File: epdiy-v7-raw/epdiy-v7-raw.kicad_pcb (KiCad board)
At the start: 4 copper layers, 128.4 x 74.9 mm, 110 parts, among them CN1 WP27D-S050VA3-R15000, IC1 MPU-6500, J1 USB_C_Receptacle_USB2.0, J2 EXTENSION_HEADER, J3 SIGNALS_HEADER, J5 CONN_BAT, J7 ESP_HDR, Q1 AO3401A, SW1 TC-0522C-1.7-160G, SW2 TC-0522C-1.7-160G, U1 RT9080-33GJ5, U10 ED060XC5, U11 TP4056, U3 TPS651851RSLR, U4 USBLC6-2P6, U8 ESP32-S3-WROOM-1, Y1 RV-3032-C7

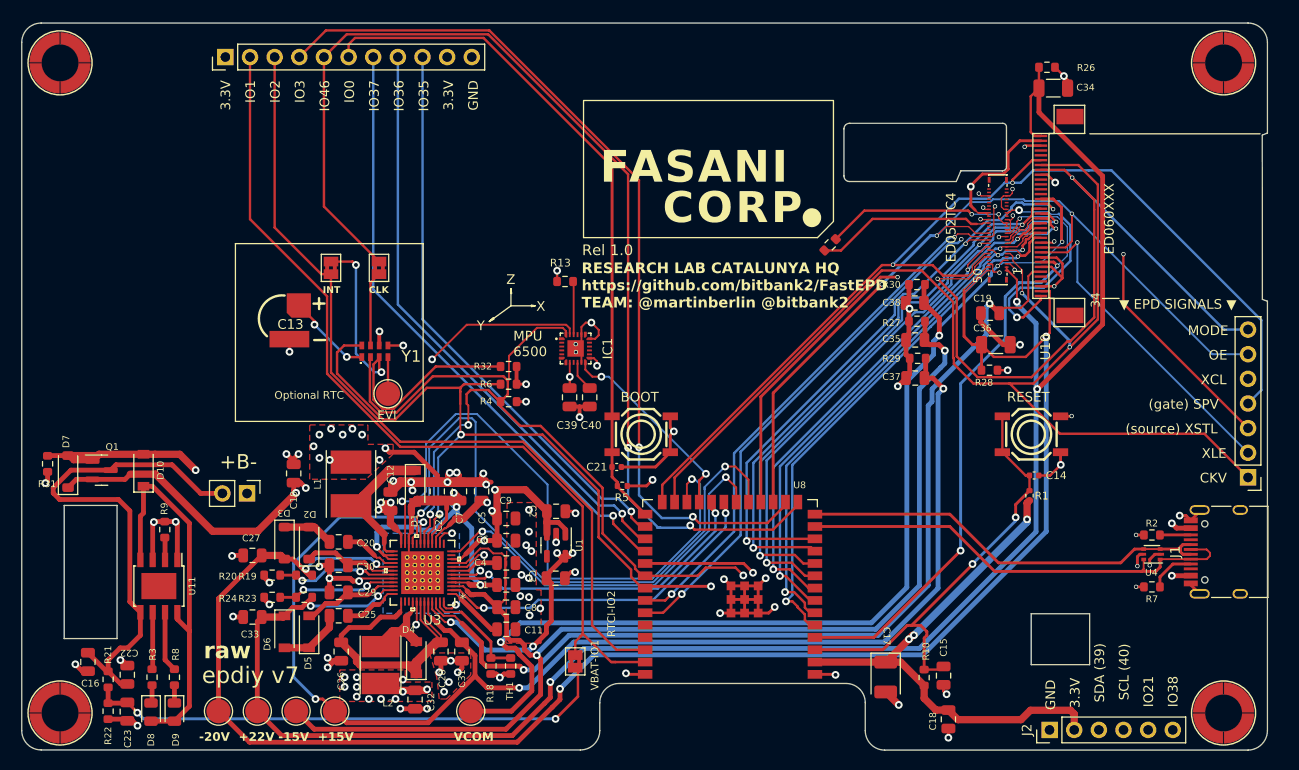
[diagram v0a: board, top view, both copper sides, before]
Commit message: Add MicroSD and fab files v1.0
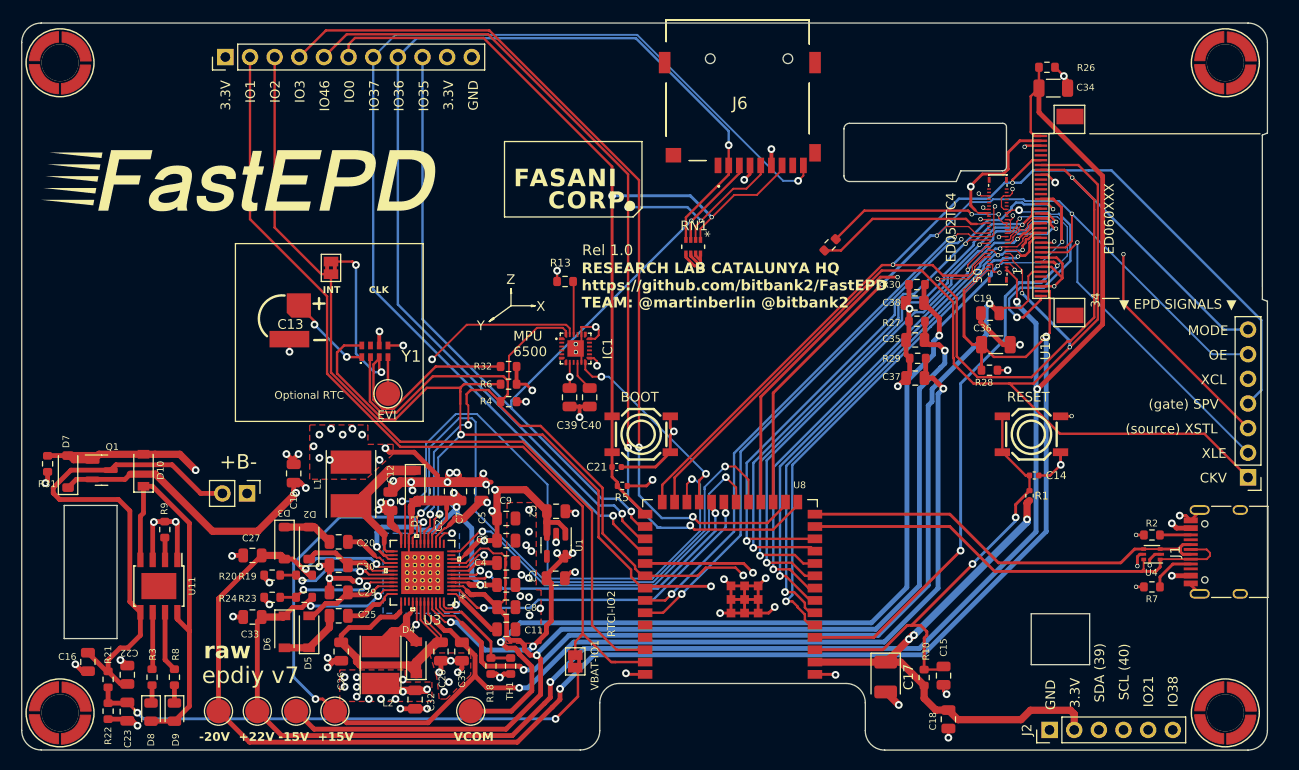
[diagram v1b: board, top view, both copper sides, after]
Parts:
- removed JP3: RTCCLK_GPIO1, Jumper:SolderJumper-2_P1.3mm_Bridged2Bar_Pad1.0x1.5mm
- added J6: THD2528-11SD-GF, footprints:MicroSD_THD252811SDGF, F.Cu at (131.8, 54.6)
- added RN1: R_Pack04, footprints:RESN_F392JTCE_UNR_SD-pullup, F.Cu at (127.2, 70.7)
- R3, R8: value 1k -> 2.4k
- R4, R6: value 10k -> 5.1k
- moved H2 0.18 mm to (182.1, 51.8)
- moved H4 0.18 mm to (182.1, 118.8)
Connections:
- Y1 pad 7: /RTC_CLK -> unconnected-(Y1-CLKOUT-Pad7)
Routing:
- net /GPIO_37: track 63.6 -> 116.4 mm, vias 1 -> 2
- net /GPIO_36: track 61.4 -> 113.3 mm, vias 1 -> 2
- net /GPIO_35: track 59.2 -> 96.0 mm, vias 1 -> 2
- net 3.3V: track 106.1 -> 140.6 mm, vias 14 -> 16
- net /IO0: track 71.5 -> 95.2 mm, vias 0 -> 2
- net /RTC_CLK: track 7.71 -> 0.00 mm
- net /GPIO_3: track 115.8 -> 111.8 mm, vias 2 -> 4
- net GND: track 200.0 -> 201.3 mm, vias 98 -> 99

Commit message: Update v7 raw
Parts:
- added R12: 10K, Resistor_SMD:R_0603_1608Metric, F.Cu at (180.8, 113.2)
- added R14: 10K, Resistor_SMD:R_0603_1608Metric, F.Cu at (62.5, 61.4)
- added R15: 10K, Resistor_SMD:R_0603_1608Metric, F.Cu at (62.5, 74.3)
- added SW3: K2-1806SQ-A2DW-04, footprints:C5143621_KEY-SMD_TS24ZJ, F.Cu at (184.5, 112.3)
- added SW4: K2-1806SQ-A2DW-04, footprints:C5143621_KEY-SMD_TS24ZJ, F.Cu at (59.8, 63.2)
- added SW5: K2-1806SQ-A2DW-04, footprints:C5143621_KEY-SMD_TS24ZJ, F.Cu at (59.8, 76.0)
- moved SW1 17.6 mm to (144.5, 88.5), turned to -90 degrees
- moved SW2 1.89 mm to (120.8, 88.5), turned to -90 degrees
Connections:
- SW1 pad 1: /EN -> GND
- SW1 pad 4: GND -> /EN
- SW2 pad 1: /IO0 -> GND
- SW2 pad 4: GND -> /IO0
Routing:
- net /GPIO_38: track 60.4 -> 132.6 mm, vias 1 -> 3
- net /GPIO_3: track 111.8 -> 173.2 mm
- net /GPIO_46: track 92.5 -> 127.9 mm
- net /EN: track 47.0 -> 65.9 mm
- net GND: track 201.3 -> 213.7 mm, vias 99 -> 102
- net Net-(R14-Pad1): track 0.00 -> 2.38 mm
- net Net-(R12-Pad1): track 0.00 -> 2.15 mm
- net Net-(R15-Pad1): track 0.00 -> 2.08 mm

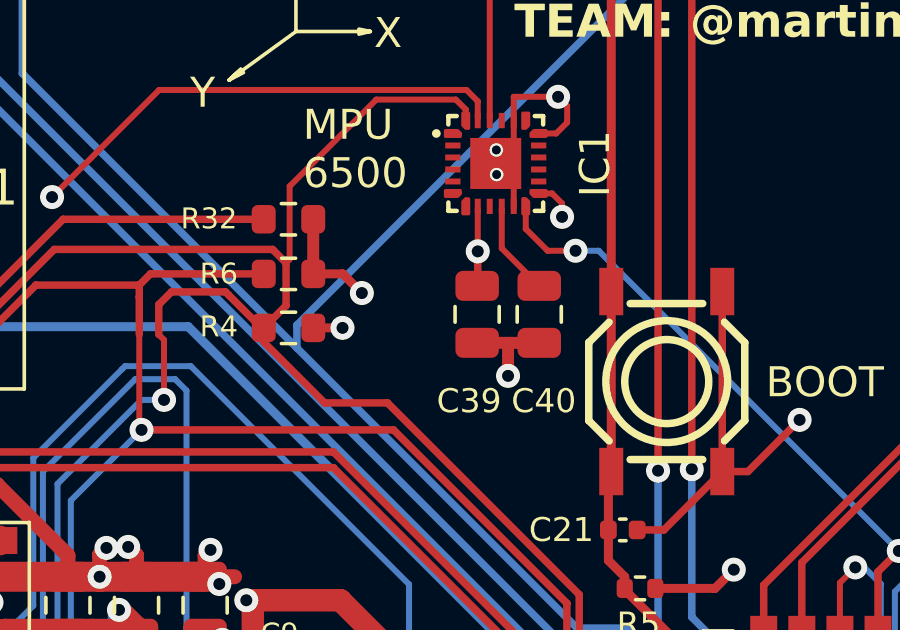
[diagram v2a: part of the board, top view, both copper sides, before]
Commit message: 1.1 corrected IMU to 0x69
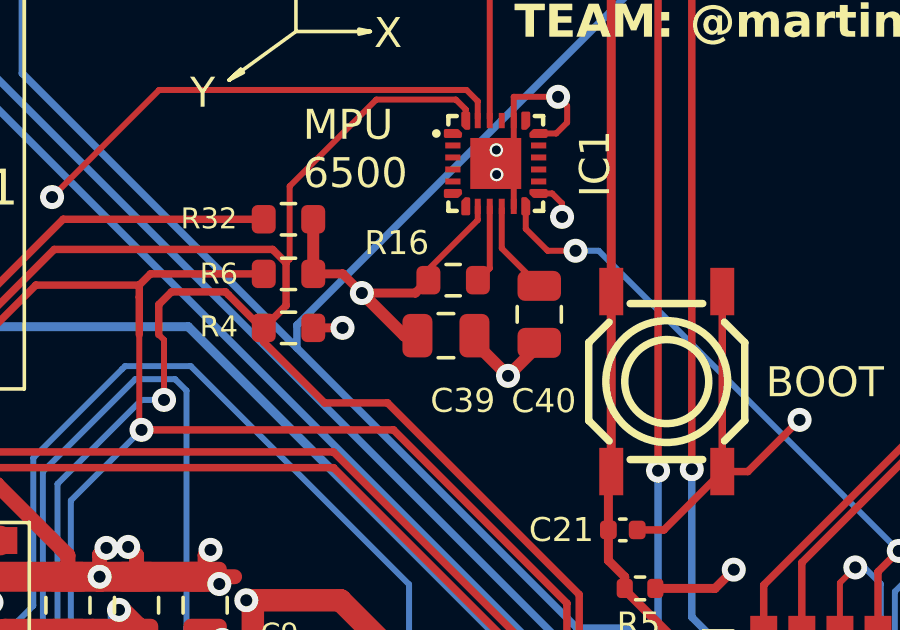
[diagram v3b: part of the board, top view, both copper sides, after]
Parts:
- added R16: 10k, Resistor_SMD:R_0603_1608Metric, F.Cu at (113.7, 85.1)
- moved C39 1.26 mm to (113.4, 87.0), turned to 180 degrees
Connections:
- IC1 pad 9: unconnected-(IC1-SDO_/_AD0-Pad9) -> /ADD_69
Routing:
- net 3.3V: track 140.6 -> 146.0 mm, vias 16 -> 15
- net /ADD_69: track 0.00 -> 2.62 mm
